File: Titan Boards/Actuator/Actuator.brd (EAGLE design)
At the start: 101.6 x 101.6 mm, 82 parts, among them Y1 16MHz, Y3 32.768kHz

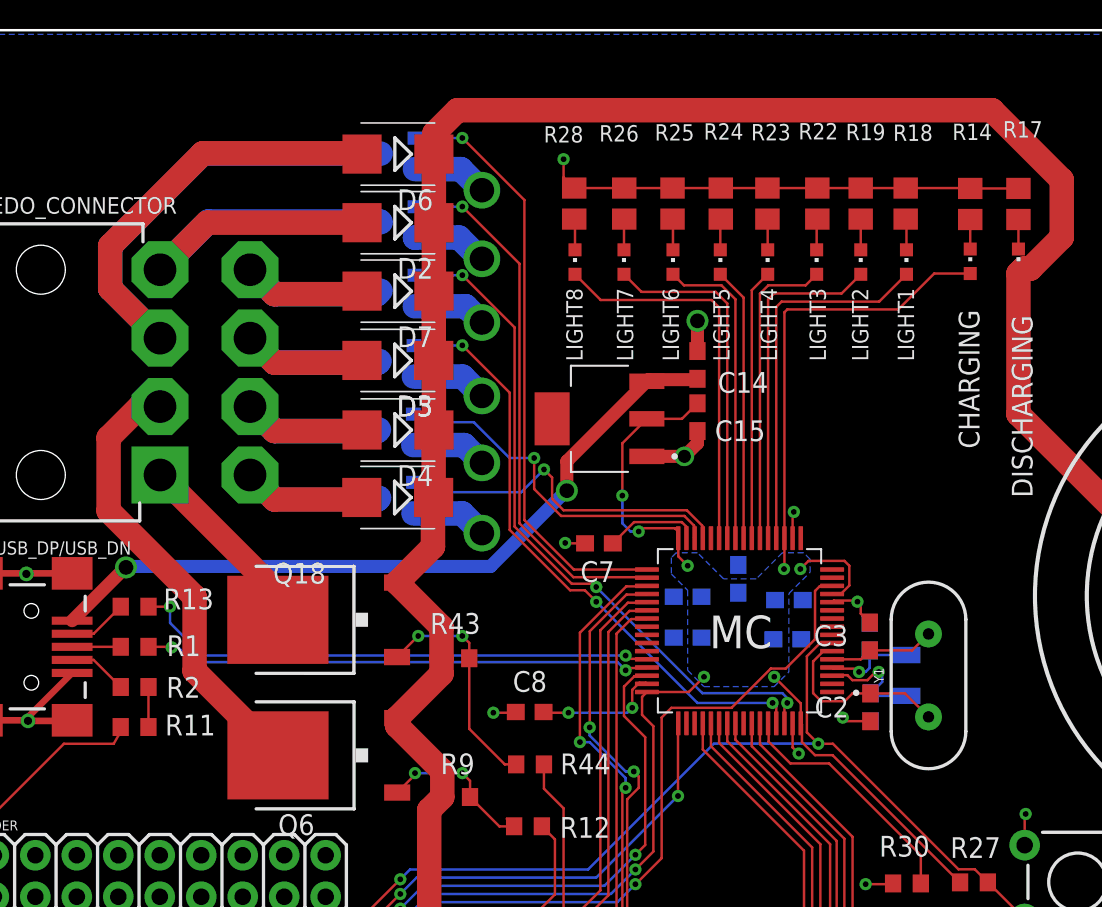
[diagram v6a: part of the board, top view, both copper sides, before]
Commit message: Actuator double MOSFET addition
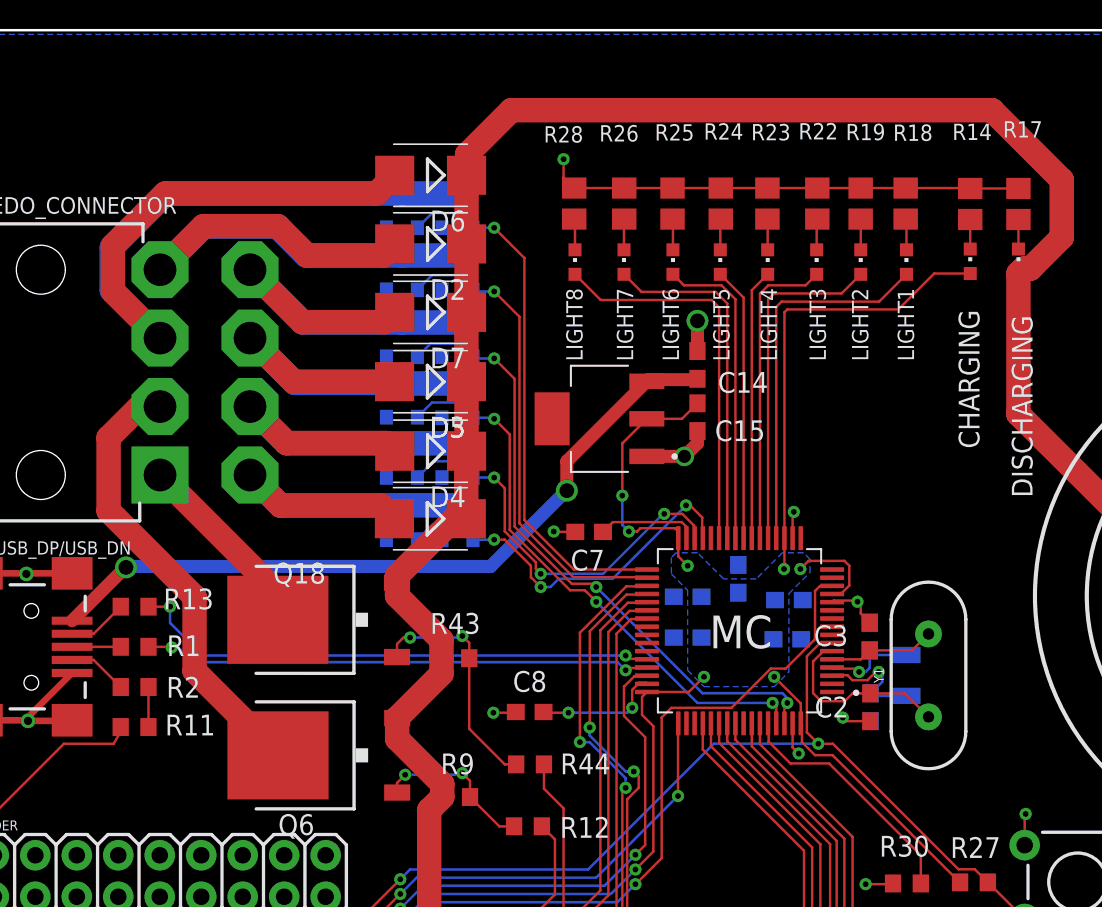
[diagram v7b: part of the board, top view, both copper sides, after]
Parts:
- added Q10, Q11, Q16, Q7, Q8, Q9: (no value), SparkFun-DiscreteSemi:SOT23-3
- moved Q1 4.78 mm to (34.2, 86.7), turned to 0 degrees
- moved Q14 4.71 mm to (34.2, 82.6), turned to 0 degrees
- moved Q4 4.42 mm to (34.2, 78.9), turned to 0 degrees
- moved Q5 4.01 mm to (34.2, 71.4), turned to 0 degrees
- moved Q15 3.55 mm to (30.8, 90.5), turned to 0 degrees
- moved D7 2.39 mm to (32.6, 84.3)
- moved D5 2.39 mm to (32.5, 80.1)
- moved D2 2.39 mm to (32.6, 88.5)
- moved D3 2.39 mm to (32.5, 71.7)
- moved D4 2.39 mm to (32.6, 75.8)
- moved D6 2.39 mm to (32.6, 92.7)
- moved Q13 1.96 mm to (30.8, 75.2), turned to 0 degrees
- moved C7 0.92 mm to (42.3, 70.9)
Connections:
- removed net AGND1: Q15.2
- net AGND: now also Q10.2, Q11.2, Q15.2, Q16.2, Q7.2, Q8.2, Q9.2
- net COIL_1: now also Q7.3
- net COIL_1_GATE: now also Q7.1
- net COIL_2: now also Q8.3
- net COIL_2_GATE: now also Q8.1
- net COIL_3: now also Q9.3
- net COIL_3_GATE: now also Q9.1
- net COIL_4: now also Q10.3
- net COIL_4_GATE: now also Q10.1
- net COIL_5: now also Q11.3
- net COIL_5_GATE: now also Q11.1
- net COIL_S: now also Q16.3
- net COIL_S_GATE: now also Q16.1
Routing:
- net AGND: track 99.5 -> 76.4 mm, vias 27 -> 22
- net COIL_2: track 16.3 -> 24.7 mm
- net COIL_S: track 28.3 -> 36.6 mm
- net COIL_1: track 16.1 -> 24.0 mm
- net COIL_4: track 16.1 -> 23.7 mm
- net COIL_3: track 16.1 -> 23.6 mm
- net COIL_5: track 50.5 -> 55.3 mm
- net AGND1: track 4.64 -> 0.00 mm, vias 1 -> 0
- net COIL_5_GATE: track 36.6 -> 32.9 mm
- net COIL_S_GATE: track 32.9 -> 29.5 mm
- net COIL_2_GATE: track 42.3 -> 38.9 mm
- net COIL_1_GATE: track 37.3 -> 34.5 mm
- net COIL_4_GATE: track 21.9 -> 24.6 mm, vias 1 -> 3
- net COIL_3_GATE: track 21.5 -> 23.5 mm, vias 1 -> 3
- net +24V: track 147.7 -> 146.3 mm

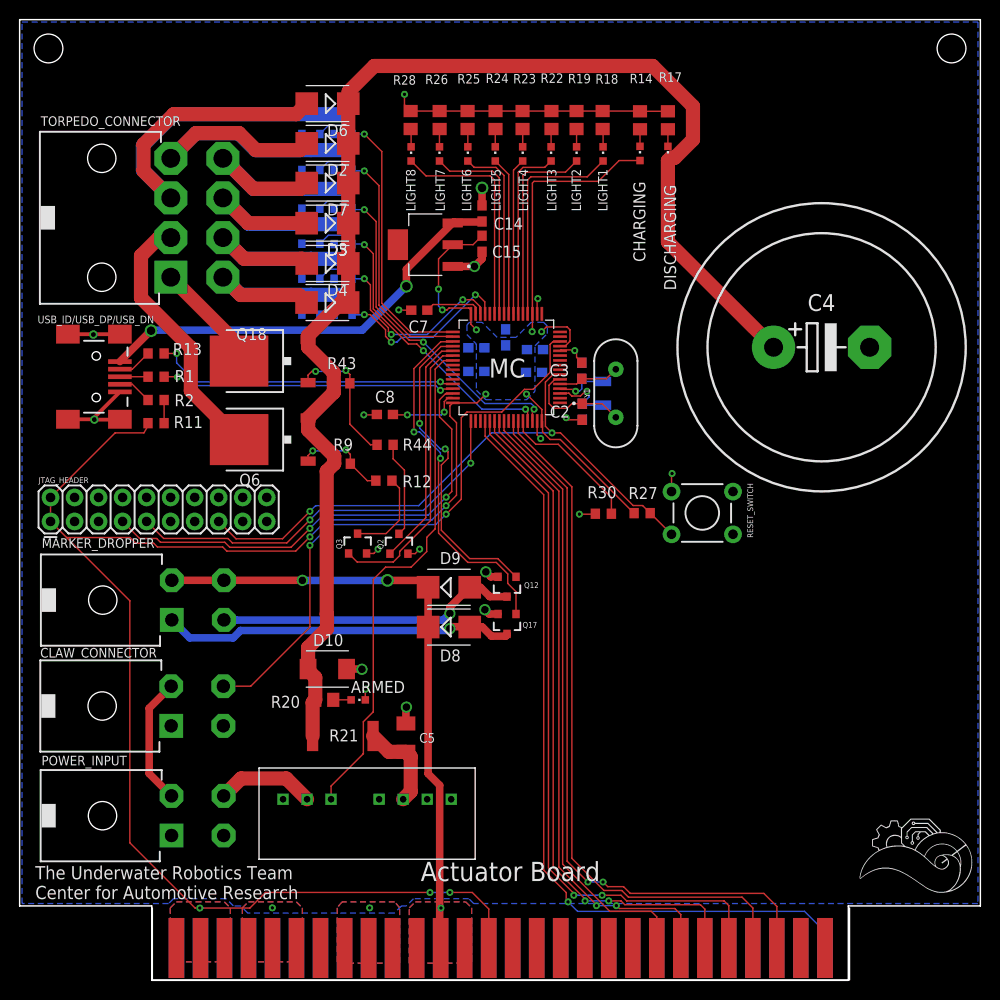
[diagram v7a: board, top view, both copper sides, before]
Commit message: Review Actuator changes, varistors
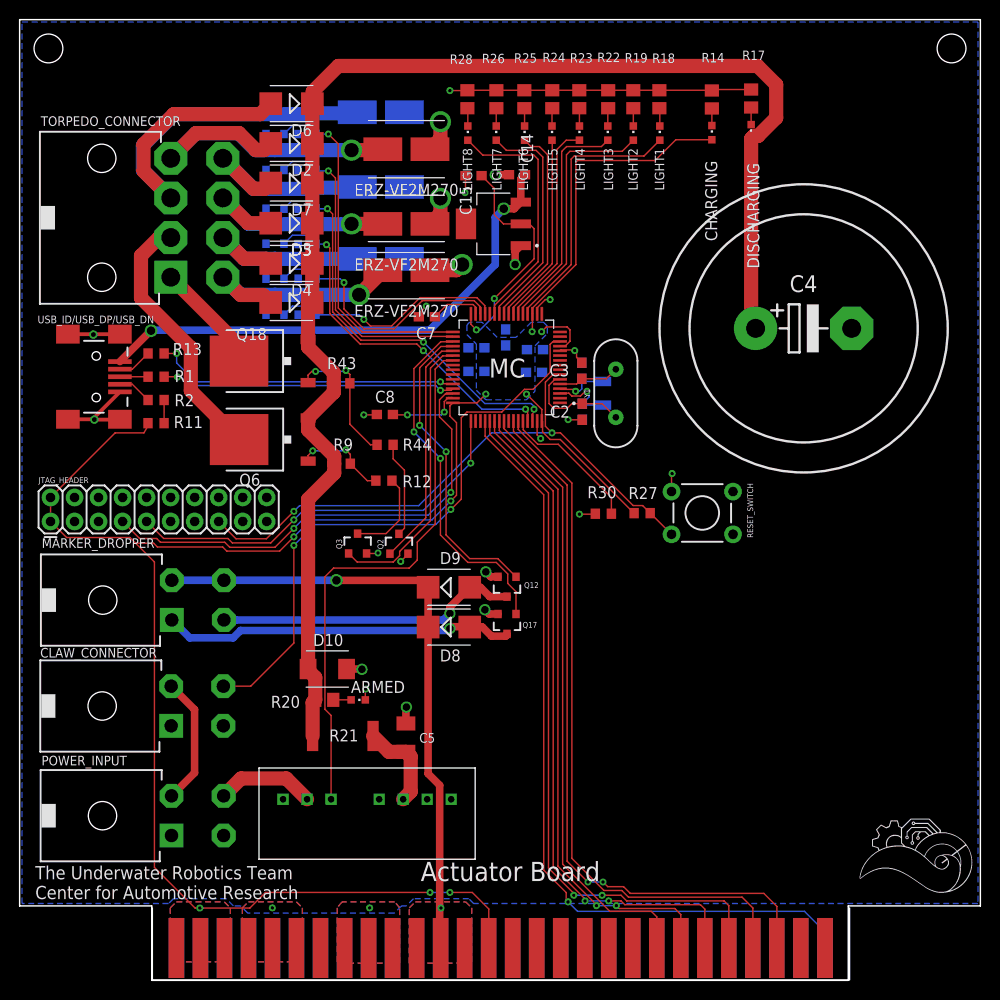
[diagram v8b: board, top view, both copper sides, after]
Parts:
- added U$2, U$3, U$4, U$5, U$7, U$8: ERZ-VF2M270ERZ-VF2M270, ERZ-VF2M270:RESM8060X320N
- moved DISCHARGING 9.10 mm to (77.4, 89.7)
- moved R17 9.10 mm to (77.4, 93.3)
- moved CHARGING 7.91 mm to (73.2, 89.6)
- moved R14 7.91 mm to (73.2, 93.2)
- moved VR1 7.53 mm to (50.1, 80.0)
- moved C15 7.26 mm to (48.0, 85.1), turned to 180 degrees
- moved LIGHT2 6.39 mm to (64.9, 89.6)
- moved R18 6.39 mm to (67.7, 93.2)
- moved R19 6.39 mm to (64.9, 93.2)
- moved R22 6.39 mm to (62.2, 93.2)
- moved R23 6.39 mm to (59.2, 93.2)
- moved R24 6.39 mm to (56.3, 93.2)
- moved R25 6.39 mm to (53.4, 93.2)
- moved R26 6.39 mm to (50.4, 93.2)
- moved R28 6.39 mm to (47.4, 93.2)
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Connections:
- net AGND: now also U$2.1, U$3.1, U$4.1, U$5.1, U$7.1, U$8.1
- net COIL_1: now also U$8.2
- net COIL_2: now also U$7.2
- net COIL_3: now also U$5.2
- net COIL_4: now also U$4.2
- net COIL_5: now also U$3.2
- net COIL_S: now also U$2.2
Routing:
- net AGND: track 76.4 -> 89.4 mm, vias 22 -> 26
- net +3V3: track 227.5 -> 239.6 mm, vias 12 -> 11
- net VBUS: track 45.5 -> 55.5 mm
- net +24V: track 146.3 -> 152.1 mm
- net LED2: track 20.9 -> 26.4 mm
- net LED4: track 16.6 -> 22.1 mm
- net LED3: track 18.9 -> 24.4 mm
- net LED1: track 23.0 -> 28.5 mm
- net COIL_2_GATE: track 38.9 -> 43.5 mm
- net COIL_S_GATE: track 29.5 -> 34.1 mm
- net COIL_5_GATE: track 32.9 -> 37.4 mm
- net COIL_1_GATE: track 34.5 -> 39.0 mm
- net ARM_TORPEDO: track 53.9 -> 57.5 mm
- net LED5: track 16.8 -> 20.3 mm
- net COIL_4_GATE: track 24.6 -> 27.7 mm, vias 3 -> 1
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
